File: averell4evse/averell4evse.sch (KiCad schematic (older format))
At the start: 15 parts, among them J1 Conn_01x16, J2 CONNFLY_Elec_DS1129-04-S8B0P-X, J3 Conn_01x04, J4 Conn_01x03, J5 Conn_01x09, U1 KT2520K-T, U2 NFCv4, U3 TLC5957RTQ, U4 74AUC2G125, U5 touch_sensor

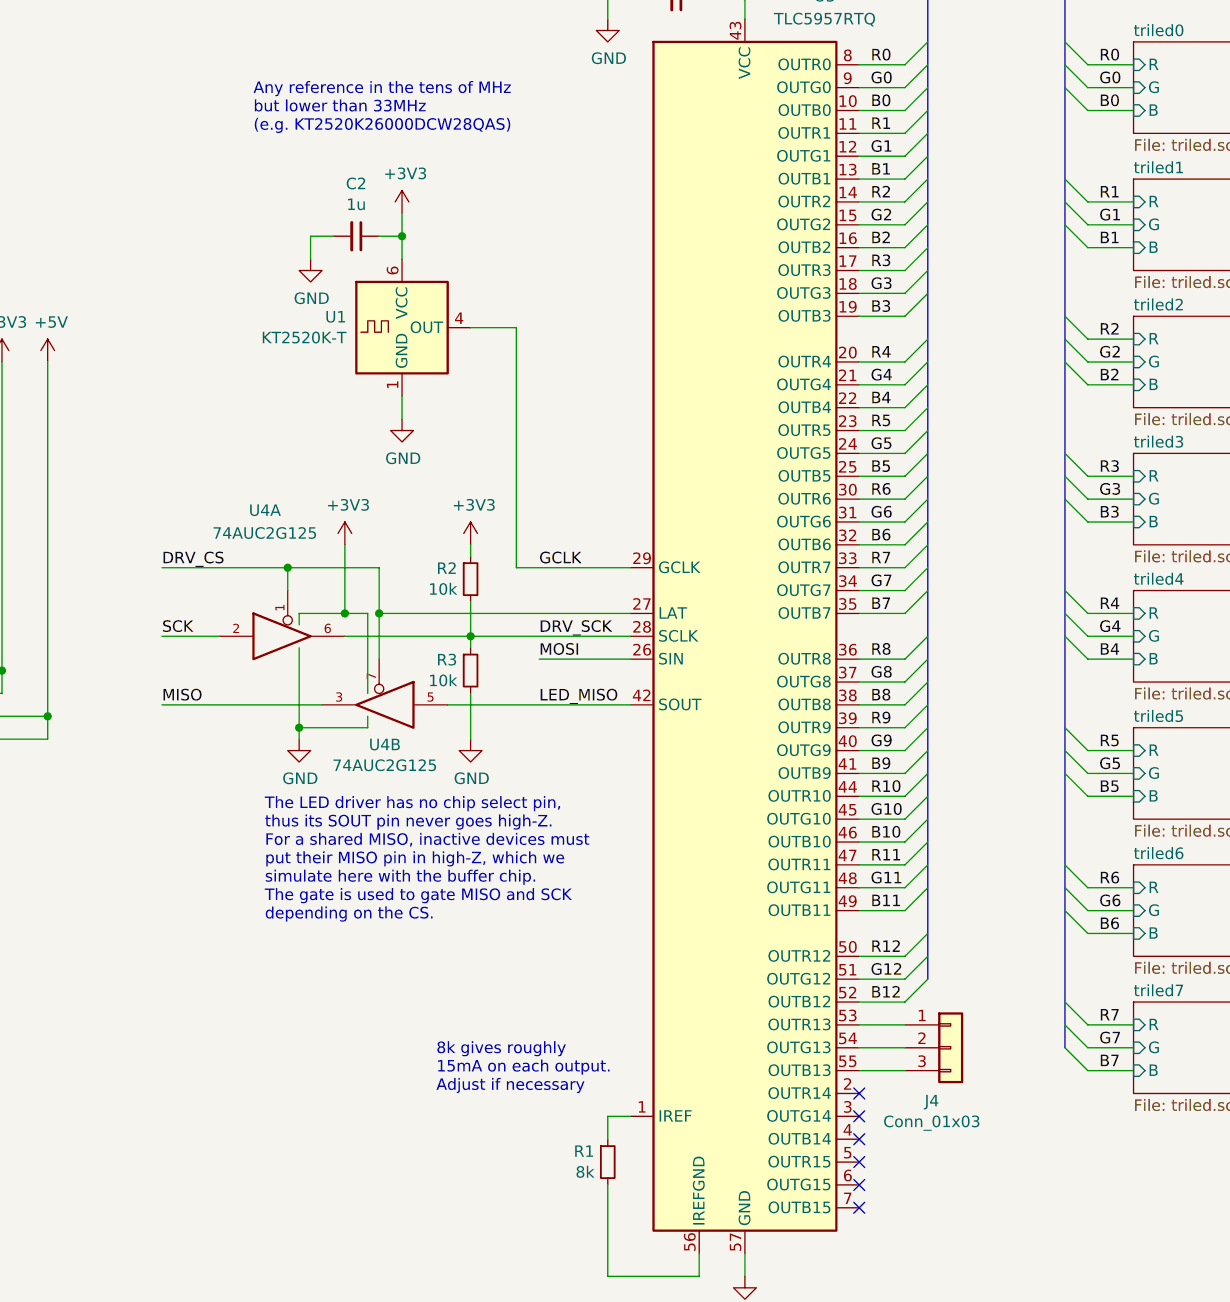
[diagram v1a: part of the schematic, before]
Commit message: averell{sch, pcb}: Change oscillator and fix improper traces
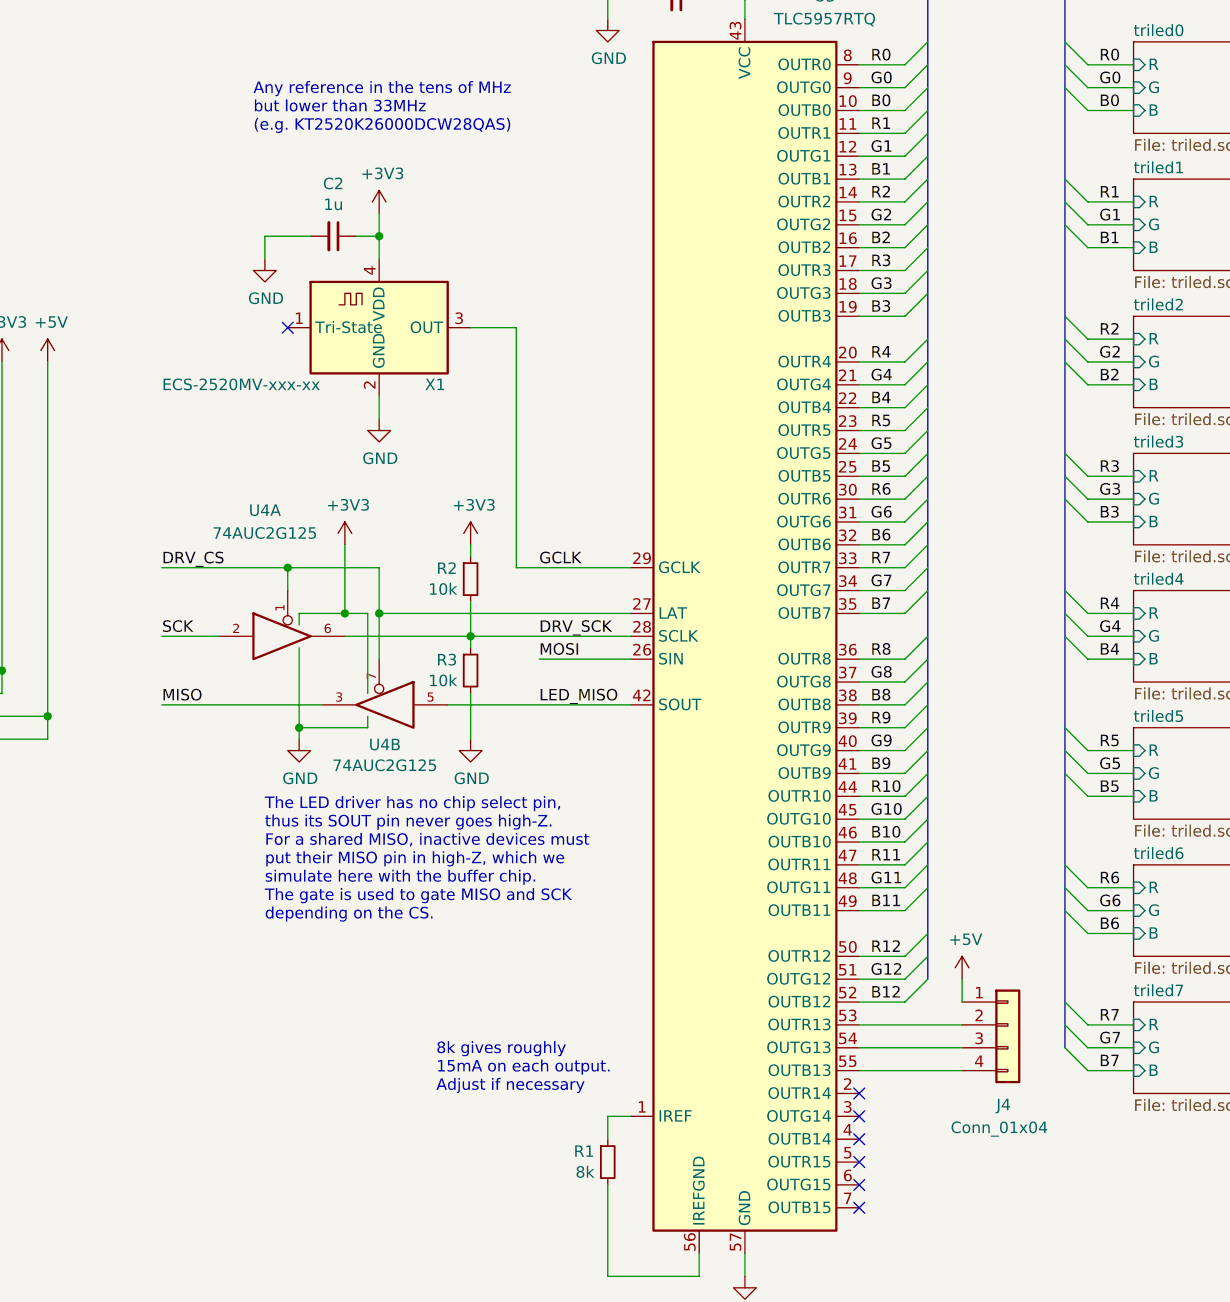
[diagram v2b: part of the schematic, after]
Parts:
- removed J4: Conn_01x03, Connector_PinHeader_2.54mm:PinHeader_1x03_P2.54mm_Horizontal, symbol Connector_Generic:Conn_01x03
- removed U1: KT2520K-T, Oscillator:Oscillator_SMD_Kyocera_2520-6Pin_2.5x2.0mm, symbol Oscillator:KT2520K-T
- added J4: Conn_01x04, Connector_PinHeader_2.54mm:PinHeader_1x04_P2.54mm_Horizontal, symbol Connector_Generic:Conn_01x04
- added X1: ECS-2520MV-xxx-xx, Oscillator:Oscillator_SMD_ECS_2520MV-xxx-xx-4Pin_2.5x2.0mm, symbol Oscillator:ECS-2520MV-xxx-xx
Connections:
- net +3V3: now also X1.4 (VDD)
- net +5V: now also J4.1 (Pin_1)
- net GCLK: now also X1.3 (OUT)
- net GND: now also X1.2 (GND)
- net at U3.53 (OUTR13): now also J4.2 (Pin_2)
- net at U3.54 (OUTG13): now also J4.3 (Pin_3)
- net at U3.55 (OUTB13): now also J4.4 (Pin_4)
- no-connect marks 16 -> 17
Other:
- moved on the sheet: C2
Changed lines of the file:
@@
 EESchema Schematic File Version 4
-LIBS:averell4evse-cache
-EELAYER 29 0
+EELAYER 30 0
 EELAYER END
 $Descr A4 11693 8268
@@
 	4800 1150 4800 1250
 $Comp
-L Oscillator:KT2520K-T U1
-U 1 1 5DC398C9
-P 3900 2600
-F 0 "U1" H 3657 2646 50  0000 R CNN
-F 1 "KT2520K-T" H 3657 2555 50  0000 R CNN
-F 2 "Oscillator:Oscillator_SMD_Kyocera_2520-6Pin_2.5x2.0mm" H 3800 2500 50  0001 C CNN
-F 3 "https://global.kyocera.com/prdct/electro/product/pdf/kt2520_e.pdf" H 3900 2600 50  0001 C CNN
-	1    3900 2600
-	1    0    0    -1
-$EndComp
-$Comp
 L power:+3V3 #PWR0104
 U 1 1 5DC3C6BA
-P 3900 2100
-F 0 "#PWR0104" H 3900 1950 50  0001 C CNN
-F 1 "+3V3" H 3915 2273 50  0000 C CNN
-F 2 "" H 3900 2100 50  0001 C CNN
-F 3 "" H 3900 2100 50  0001 C CNN
-	1    3900 2100
+P 3800 2100
+F 0 "#PWR0104" H 3800 1950 50  0001 C CNN
+F 1 "+3V3" H 3815 2273 50  0000 C CNN
+F 2 "" H 3800 2100 50  0001 C CNN
+F 3 "" H 3800 2100 50  0001 C CNN
+	1    3800 2100
 	1    0    0    -1
 $EndComp
@@
 L power:GND #PWR0105
 U 1 1 5DC3CF81
-P 3900 3000
-F 0 "#PWR0105" H 3900 2750 50  0001 C CNN
-F 1 "GND" H 3905 2827 50  0000 C CNN
-F 2 "" H 3900 3000 50  0001 C CNN
-F 3 "" H 3900 3000 50  0001 C CNN
-	1    3900 3000
+P 3800 3000
+F 0 "#PWR0105" H 3800 2750 50  0001 C CNN
+F 1 "GND" H 3805 2827 50  0000 C CNN
+F 2 "" H 3800 3000 50  0001 C CNN
+F 3 "" H 3800 3000 50  0001 C CNN
+	1    3800 3000
 	1    0    0    -1
 $EndComp
@@
 L Device:C_Small C2
 U 1 1 5DC3D87A
-P 3700 2200
-F 0 "C2" V 3471 2200 50  0000 C CNN
-F 1 "1u" V 3562 2200 50  0000 C CNN
-F 2 "Capacitor_SMD:C_0603_1608Metric" H 3700 2200 50  0001 C CNN
-F 3 "~" H 3700 2200 50  0001 C CNN
-	1    3700 2200
+P 3600 2200
+F 0 "C2" V 3371 2200 50  0000 C CNN
+F 1 "1u" V 3462 2200 50  0000 C CNN
+F 2 "Capacitor_SMD:C_0603_1608Metric" H 3600 2200 50  0001 C CNN
+F 3 "~" H 3600 2200 50  0001 C CNN
+	1    3600 2200
 	0    1    1    0
 $EndComp
@@
 L power:GND #PWR0106
 U 1 1 5DC403E4
-P 3500 2300
-F 0 "#PWR0106" H 3500 2050 50  0001 C CNN
-F 1 "GND" H 3505 2127 50  0000 C CNN
-F 2 "" H 3500 2300 50  0001 C CNN
-F 3 "" H 3500 2300 50  0001 C CNN
-	1    3500 2300
-	1    0    0    -1
-$EndComp
-Wire Wire Line
-	3600 2200 3500 2200
-Wire Wire Line
-	3500 2200 3500 2300
-Wire Wire Line
-	3800 2200 3900 2200
-Wire Wire Line
-	3900 2200 3900 2100
-Connection ~ 3900 2200
-Wire Wire Line
-	3900 2200 3900 2300
-Wire Wire Line
-	3900 2900 3900 3000
+P 3300 2300
+F 0 "#PWR0106" H 3300 2050 50  0001 C CNN
+F 1 "GND" H 3305 2127 50  0000 C CNN
+F 2 "" H 3300 2300 50  0001 C CNN
+F 3 "" H 3300 2300 50  0001 C CNN
+	1    3300 2300
+	1    0    0    -1
+$EndComp
+Wire Wire Line
+	3500 2200 3300 2200
+Wire Wire Line
+	3300 2200 3300 2300
+Wire Wire Line
+	3700 2200 3800 2200
+Wire Wire Line
+	3800 2200 3800 2100
+Connection ~ 3800 2200
+Wire Wire Line
+	3800 2200 3800 2300
+Wire Wire Line
+	3800 2900 3800 3000
 Text Label 4500 3650 0    50   ~ 0
 GCLK
@@
 	10050 5100 10450 5100
 Wire Wire Line
-	5900 5650 6100 5650
-Wire Wire Line
-	5900 5750 6100 5750
-Wire Wire Line
-	5900 5850 6100 5850
+	5900 5650 6350 5650
+Wire Wire Line
+	5900 5750 6350 5750
+Wire Wire Line
+	5900 5850 6350 5850
 $Sheet
 S 7100 1950 550  400
@@
 $EndComp
 $Comp
-L Connector_Generic:Conn_01x03 J4
-U 1 1 5DDA55B8
-P 6300 5750
-F 0 "J4" H 6218 5517 50  0000 C CNN
-F 1 "Conn_01x03" H 6218 5426 50  0000 C CNN
-F 2 "Connector_PinHeader_2.54mm:PinHeader_1x03_P2.54mm_Horizontal" H 6300 5750 50  0001 C CNN
-F 3 "~" H 6300 5750 50  0001 C CNN
-	1    6300 5750
-	1    0    0    -1
-$EndComp
-$Comp
 L Connector_Generic:Conn_01x09 J5
 U 1 1 5DDB2582
@@
 Wire Wire Line
 	1650 3300 1750 3300
+$Comp
+L Oscillator:ECS-2520MV-xxx-xx X1
+U 1 1 5E6A0EE8
+P 3800 2600
+F 0 "X1" H 4000 2350 50  0000 L CNN
+F 1 "ECS-2520MV-xxx-xx" H 2850 2350 50  0000 L CNN
+F 2 "Oscillator:Oscillator_SMD_ECS_2520MV-xxx-xx-4Pin_2.5x2.0mm" H 4250 2250 50  0001 C CNN
+F 3 "https://www.ecsxtal.com/store/pdf/ECS-2520MV.pdf" H 3625 2725 50  0001 C CNN
+	1    3800 2600
+	1    0    0    -1
+$EndComp
+NoConn ~ 3400 2600
+$Comp
+L Connector_Generic:Conn_01x04 J4
+U 1 1 5E6EDDFC
+P 6550 5650
+F 0 "J4" H 6500 5300 50  0000 L CNN
+F 1 "Conn_01x04" H 6300 5200 50  0000 L CNN
+F 2 "Connector_PinHeader_2.54mm:PinHeader_1x04_P2.54mm_Horizontal" H 6550 5650 50  0001 C CNN
+F 3 "~" H 6550 5650 50  0001 C CNN
+	1    6550 5650
+	1    0    0    -1
+$EndComp
+Wire Wire Line
+	6350 5450 6350 5550
+$Comp
+L power:+5V #PWR?
+U 1 1 5E72790F
+P 6350 5450
+F 0 "#PWR?" H 6350 5300 50  0001 C CNN
+F 1 "+5V" H 6365 5623 50  0000 C CNN
+F 2 "" H 6350 5450 50  0001 C CNN
+F 3 "" H 6350 5450 50  0001 C CNN
+	1    6350 5450
+	1    0    0    -1
+$EndComp
 Wire Bus Line
 	8250 1050 8250 3450

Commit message: averell/*: Remove LED driver CS thingy
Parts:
- removed R2, R3: 10k, Resistor_SMD:R_0603_1608Metric, symbol Device:R_Small
- removed U4: 74AUC2G125, Package_SO:TSSOP-8_3x3mm_P0.65mm, symbol 74xGxx:74AUC2G125
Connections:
- net DRV_SCK is gone; now on net SCK: U3.28 (SCLK)
- net DRV_CS renamed DRV_LAT
- net LED_MISO: no longer names the net of U3.42 (SOUT)
- no-connect marks 17 -> 18
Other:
- note added: "Any reference in the tens of MHz\nbut lower than 33MHz\n(e.g. ECS-2520MV-120-BN-TR)"
- note removed: "Any reference in the tens of MHz\nbut lower than 33MHz\n(e.g. KT2520K26000DCW28QAS)"
- note removed: "The LED driver has no chip select pin,\nthus its SOUT pin never goes high-Z.\nFor a shared MISO, inactive devices must\nput their MISO pin in high-Z, which we\nsimulate here with the buffer chip.\nThe gate is used to gate MISO and SCK\ndepending on the CS."
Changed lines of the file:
@@
 Text Label 4500 3650 0    50   ~ 0
 GCLK
-Text Label 2850 3950 0    50   ~ 0
-SCK
 Wire Wire Line
 	4900 4050 4500 4050
@@
 Text Label 8350 4600 0    50   ~ 0
 NFC_CS
-Text Label 4500 4250 0    50   ~ 0
-LED_MISO
 Text Notes 3250 1750 0    50   ~ 0
-Any reference in the tens of MHz\nbut lower than 33MHz\n(e.g. KT2520K26000DCW28QAS)
-Wire Wire Line
-	4100 4250 4900 4250
+Any reference in the tens of MHz\nbut lower than 33MHz\n(e.g.  ECS-2520MV-120-BN-TR)
 Wire Wire Line
 	4200 2600 4400 2600
@@
 Wire Wire Line
 	4400 3650 4900 3650
-Wire Wire Line
-	2850 4250 3550 4250
-Text Label 2850 4250 0    50   ~ 0
-MISO
 Wire Wire Line
 	10050 5200 10900 5200
@@
 Text Notes 9050 3250 0    50   ~ 0
 To logo LEDs
-Text Notes 3300 5200 0    50   ~ 0
-The LED driver has no chip select pin,\nthus its SOUT pin never goes high-Z.\nFor a shared MISO, inactive devices must\nput their MISO pin in high-Z, which we\nsimulate here with the buffer chip.\nThe gate is used to gate MISO and SCK\ndepending on the CS.
 Wire Wire Line
 	10050 4300 10450 4300
@@
 Text Label 10100 5100 0    50   ~ 0
 SIGIN
-$Comp
-L 74xGxx:74AUC2G125 U4
-U 1 1 5DE55BF0
-P 3400 3950
-F 0 "U4" H 3300 4500 50  0000 C CNN
-F 1 "74AUC2G125" H 3300 4400 50  0000 C CNN
-F 2 "Package_SO:TSSOP-8_3x3mm_P0.65mm" H 3400 3950 50  0001 C CNN
-F 3 "http://www.ti.com/lit/sg/scyt129e/scyt129e.pdf" H 3400 3950 50  0001 C CNN
-	1    3400 3950
-	1    0    0    -1
-$EndComp
-$Comp
-L 74xGxx:74AUC2G125 U4
-U 2 1 5DE573F2
-P 3800 4250
-F 0 "U4" H 3775 4075 50  0000 C CNN
-F 1 "74AUC2G125" H 3775 3984 50  0000 C CNN
-F 2 "Package_SO:TSSOP-8_3x3mm_P0.65mm" H 3800 4250 50  0001 C CNN
-F 3 "http://www.ti.com/lit/sg/scyt129e/scyt129e.pdf" H 3800 4250 50  0001 C CNN
-	2    3800 4250
-	-1   0    0    -1
-$EndComp
-Wire Wire Line
-	3650 3950 4200 3950
-Wire Wire Line
-	3100 3950 2850 3950
-Wire Wire Line
-	3800 3850 4900 3850
-Connection ~ 3800 3850
-Wire Wire Line
-	3800 3850 3800 4050
-Wire Wire Line
-	3400 3750 3400 3650
-Wire Wire Line
-	3400 3650 3800 3650
-Wire Wire Line
-	3800 3650 3800 3850
-Wire Wire Line
-	3400 3650 2850 3650
-Connection ~ 3400 3650
-Text Label 2850 3650 0    50   ~ 0
-DRV_CS
-$Comp
-L power:GND #PWR0111
-U 1 1 5DF09DDB
-P 3450 4400
-F 0 "#PWR0111" H 3450 4150 50  0001 C CNN
-F 1 "GND" H 3455 4227 50  0000 C CNN
-F 2 "" H 3450 4400 50  0001 C CNN
-F 3 "" H 3450 4400 50  0001 C CNN
-	1    3450 4400
-	1    0    0    -1
-$EndComp
-Wire Wire Line
-	3450 4000 3450 4350
-Wire Wire Line
-	3450 4350 3750 4350
-Wire Wire Line
-	3750 4350 3750 4300
-Wire Wire Line
-	3450 4350 3450 4400
-Connection ~ 3450 4350
-Wire Wire Line
-	3750 4200 3750 3850
-Wire Wire Line
-	3750 3850 3650 3850
-Wire Wire Line
-	3450 3850 3450 3900
-$Comp
-L power:+3V3 #PWR0112
-U 1 1 5DF6CFFF
-P 3650 3550
-F 0 "#PWR0112" H 3650 3400 50  0001 C CNN
-F 1 "+3V3" H 3665 3723 50  0000 C CNN
-F 2 "" H 3650 3550 50  0001 C CNN
-F 3 "" H 3650 3550 50  0001 C CNN
-	1    3650 3550
-	1    0    0    -1
-$EndComp
-Wire Wire Line
-	3650 3850 3650 3550
-Connection ~ 3650 3850
-Wire Wire Line
-	3650 3850 3450 3850
-$Comp
-L Device:R_Small R2
-U 1 1 5DF98E8B
-P 4200 3700
-F 0 "R2" H 4142 3746 50  0000 R CNN
-F 1 "10k" H 4142 3655 50  0000 R CNN
-F 2 "Resistor_SMD:R_0603_1608Metric" H 4200 3700 50  0001 C CNN
-F 3 "~" H 4200 3700 50  0001 C CNN
-	1    4200 3700
-	1    0    0    -1
-$EndComp
-$Comp
-L Device:R_Small R3
-U 1 1 5DF99D5D
-P 4200 4100
-F 0 "R3" H 4142 4146 50  0000 R CNN
-F 1 "10k" H 4142 4055 50  0000 R CNN
-F 2 "Resistor_SMD:R_0603_1608Metric" H 4200 4100 50  0001 C CNN
-F 3 "~" H 4200 4100 50  0001 C CNN
-	1    4200 4100
-	1    0    0    -1
-$EndComp
-$Comp
-L power:GND #PWR010
-U 1 1 5DFA597D
-P 4200 4400
-F 0 "#PWR010" H 4200 4150 50  0001 C CNN
-F 1 "GND" H 4205 4227 50  0000 C CNN
-F 2 "" H 4200 4400 50  0001 C CNN
-F 3 "" H 4200 4400 50  0001 C CNN
-	1    4200 4400
-	1    0    0    -1
-$EndComp
-$Comp
-L power:+3V3 #PWR09
-U 1 1 5DFA60A3
-P 4200 3550
-F 0 "#PWR09" H 4200 3400 50  0001 C CNN
-F 1 "+3V3" H 4215 3723 50  0000 C CNN
-F 2 "" H 4200 3550 50  0001 C CNN
-F 3 "" H 4200 3550 50  0001 C CNN
-	1    4200 3550
-	1    0    0    -1
-$EndComp
-Wire Wire Line
-	4200 3550 4200 3600
-Wire Wire Line
-	4200 3800 4200 3950
-Connection ~ 4200 3950
-Wire Wire Line
-	4200 3950 4900 3950
-Wire Wire Line
-	4200 3950 4200 4000
-Wire Wire Line
-	4200 4200 4200 4400
+Wire Wire Line
+	4500 3850 4900 3850
 Text Label 4500 3950 0    50   ~ 0
-DRV_SCK
+SCK
 Text Label 2100 2800 2    50   ~ 0
 SCK
@@
 NFC_CS
 Text Label 2100 3500 2    50   ~ 0
-DRV_CS
+DRV_LAT
 $Comp
 L power:GND #PWR013
@@
 	6350 5450 6350 5550
 $Comp
-L power:+5V #PWR?
+L power:+5V #PWR0111
 U 1 1 5E72790F
 P 6350 5450
-F 0 "#PWR?" H 6350 5300 50  0001 C CNN
+F 0 "#PWR0111" H 6350 5300 50  0001 C CNN
 F 1 "+5V" H 6365 5623 50  0000 C CNN
 F 2 "" H 6350 5450 50  0001 C CNN
@@
 	1    0    0    -1
 $EndComp
+Text Label 4500 3850 0    50   ~ 0
+DRV_LAT
+NoConn ~ 4900 4250
+Wire Wire Line
+	4500 3950 4900 3950
 Wire Bus Line
 	8250 1050 8250 3450
